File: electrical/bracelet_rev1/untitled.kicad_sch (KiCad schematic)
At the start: 2 parts, among them U9 nRF7002-QFXX

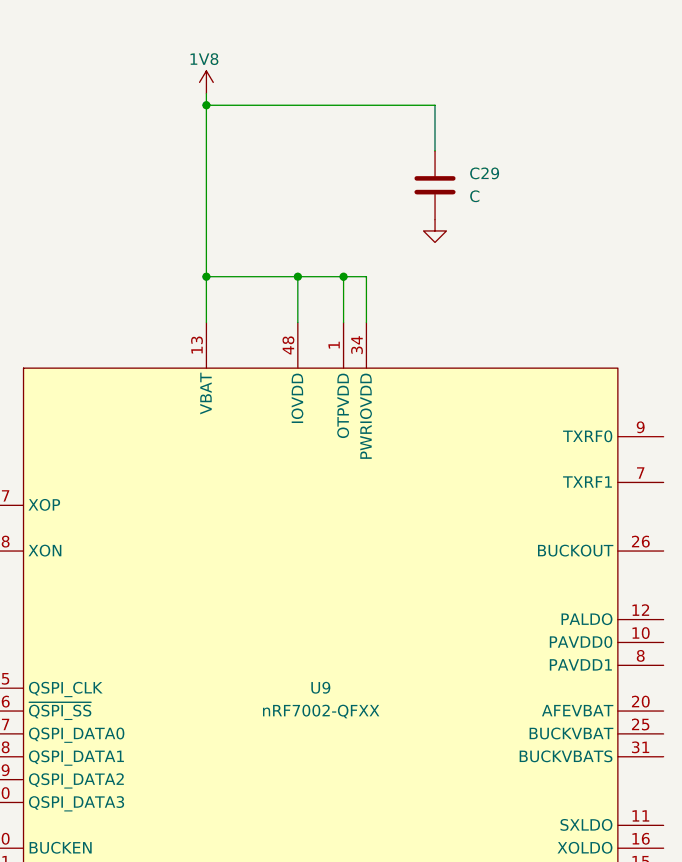
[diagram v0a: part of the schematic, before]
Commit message: Redo component numbers
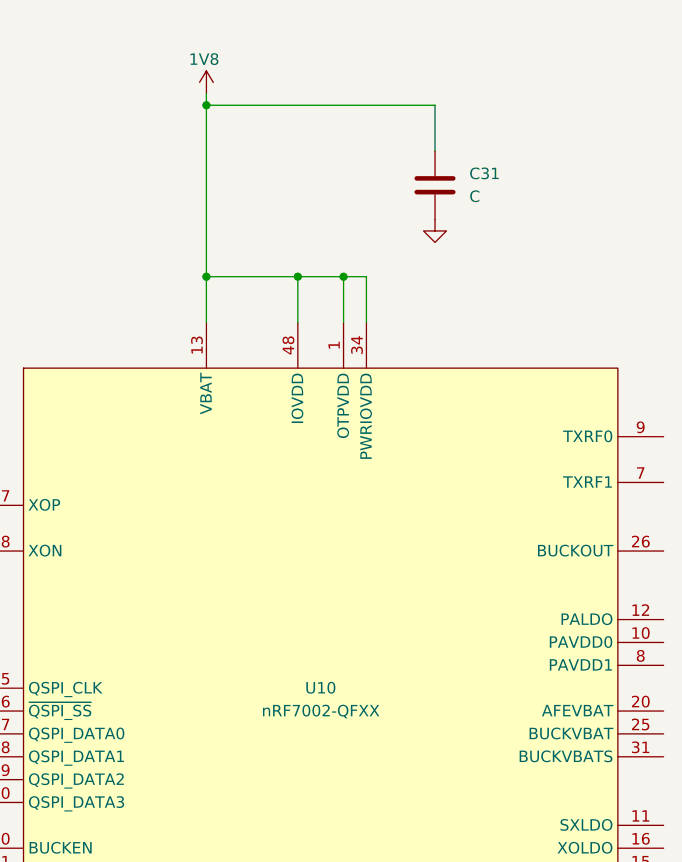
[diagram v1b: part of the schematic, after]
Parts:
- renumbered C29 to C31, U9 to U10
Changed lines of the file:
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@@
 		(dnp no)
 		(fields_autoplaced yes)
-		(property "Reference" "#PWR043"
+		(property "Reference" "#PWR?"
 			(at 152.4 52.07 0)
 			(effects
@@
 			(project "bracelet_rev1"
 				(path "/2a7dd2e8-59c9-4d04-9427-958ca4ea7daa/3d584547-2e56-41a9-bdec-87f8247f577d"
-					(reference "#PWR043")
+					(reference "#PWR?")
 					(unit 1)
 				)
@@
 		(on_board yes)
 		(dnp no)
-		(property "Reference" "#PWR067"
+		(property "Reference" "#PWR?"
 			(at 34.29 26.67 0)
 			(effects
@@
 			(project "bracelet_rev1"
 				(path "/2a7dd2e8-59c9-4d04-9427-958ca4ea7daa/3d584547-2e56-41a9-bdec-87f8247f577d"
-					(reference "#PWR067")
+					(reference "#PWR?")
 					(unit 1)
 				)
@@
 		(dnp no)
 		(fields_autoplaced yes)
-		(property "Reference" "#PWR069"
+		(property "Reference" "#PWR?"
 			(at 139.7 144.78 0)
 			(effects
@@
 			(project "bracelet_rev1"
 				(path "/2a7dd2e8-59c9-4d04-9427-958ca4ea7daa/3d584547-2e56-41a9-bdec-87f8247f577d"
-					(reference "#PWR069")
+					(reference "#PWR?")
 					(unit 1)
 				)
@@
 		(dnp no)
 		(fields_autoplaced yes)
-		(property "Reference" "C29"
+		(property "Reference" "C31"
 			(at 156.21 40.6399 0)
 			(effects
@@
 			(project ""
 				(path "/2a7dd2e8-59c9-4d04-9427-958ca4ea7daa/3d584547-2e56-41a9-bdec-87f8247f577d"
-					(reference "C29")
+					(reference "C31")
 					(unit 1)
 				)
@@
 		(dnp no)
 		(fields_autoplaced yes)
-		(property "Reference" "U9"
+		(property "Reference" "U10"
 			(at 139.7 97.79 0)
 			(do_not_autoplace yes)
@@
 			(project "bracelet_rev1"
 				(path "/2a7dd2e8-59c9-4d04-9427-958ca4ea7daa/3d584547-2e56-41a9-bdec-87f8247f577d"
-					(reference "U9")
+					(reference "U10")
 					(unit 1)
 				)
@@
 		(on_board yes)
 		(dnp no)
-		(property "Reference" "#PWR068"
+		(property "Reference" "#PWR?"
 			(at 127 35.56 0)
 			(effects
@@
 			(project "bracelet_rev1"
 				(path "/2a7dd2e8-59c9-4d04-9427-958ca4ea7daa/3d584547-2e56-41a9-bdec-87f8247f577d"
-					(reference "#PWR068")
-					(unit 1)
-				)
+					(reference "#PWR?")
+					(unit 1)
+				)

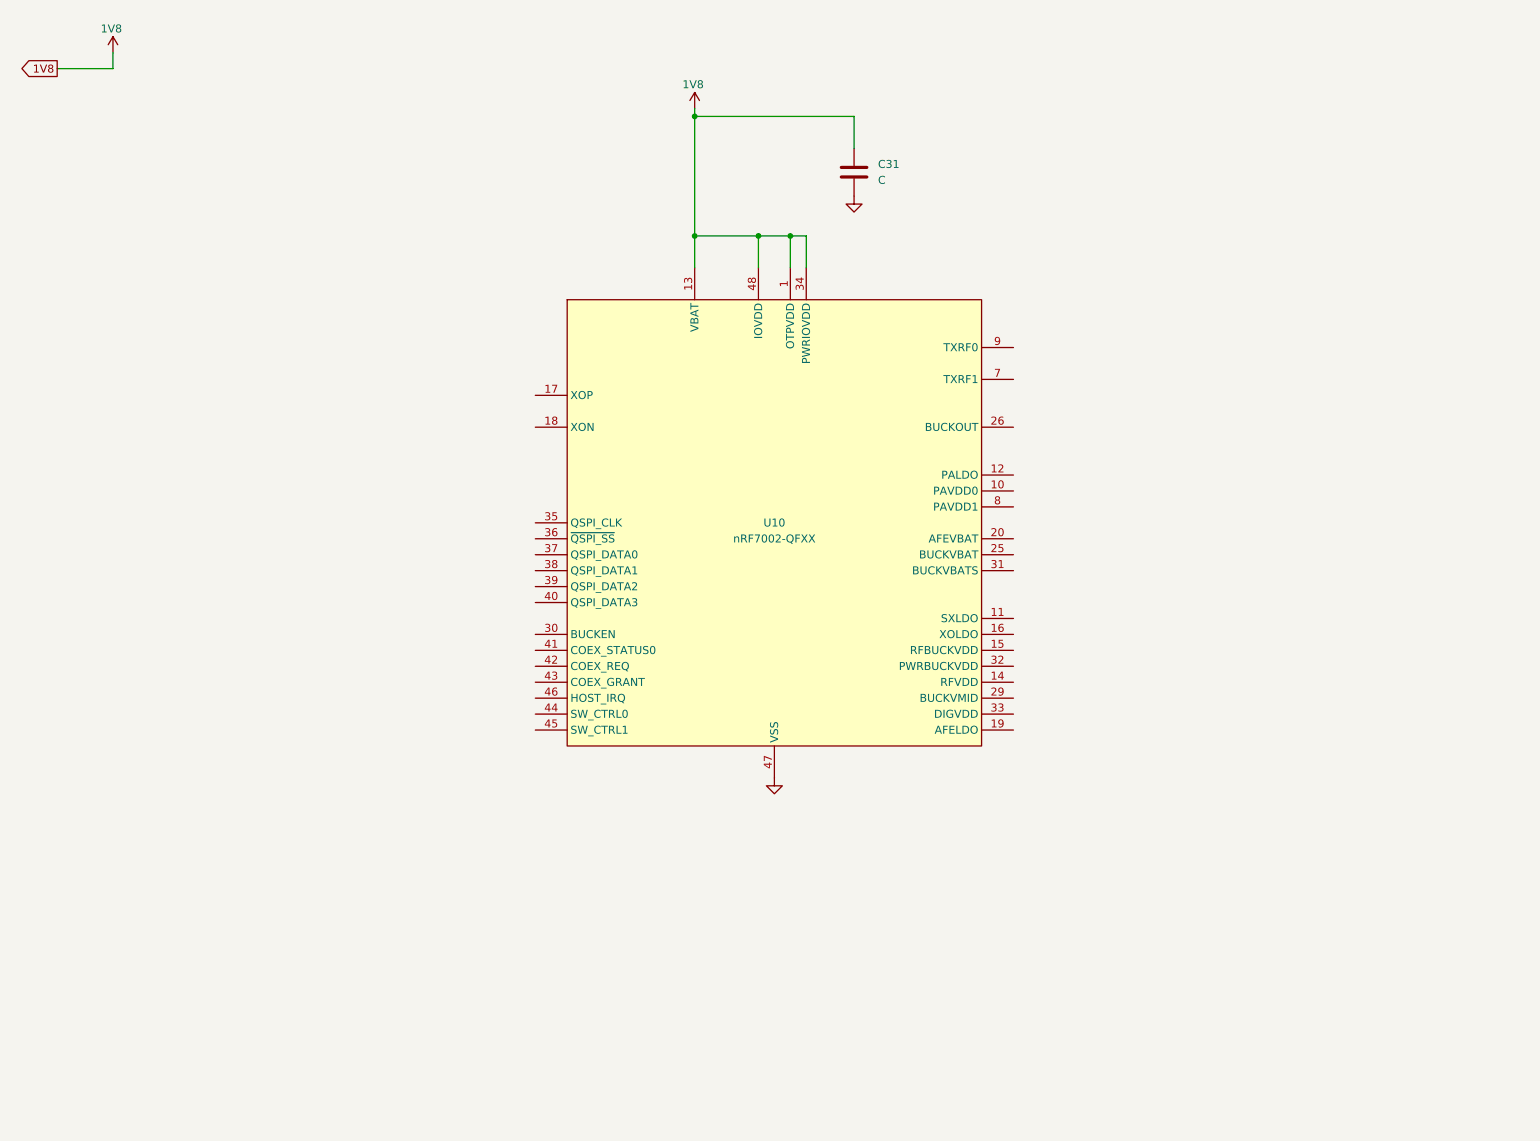
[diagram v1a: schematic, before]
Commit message: Updated Wi-Fi IC
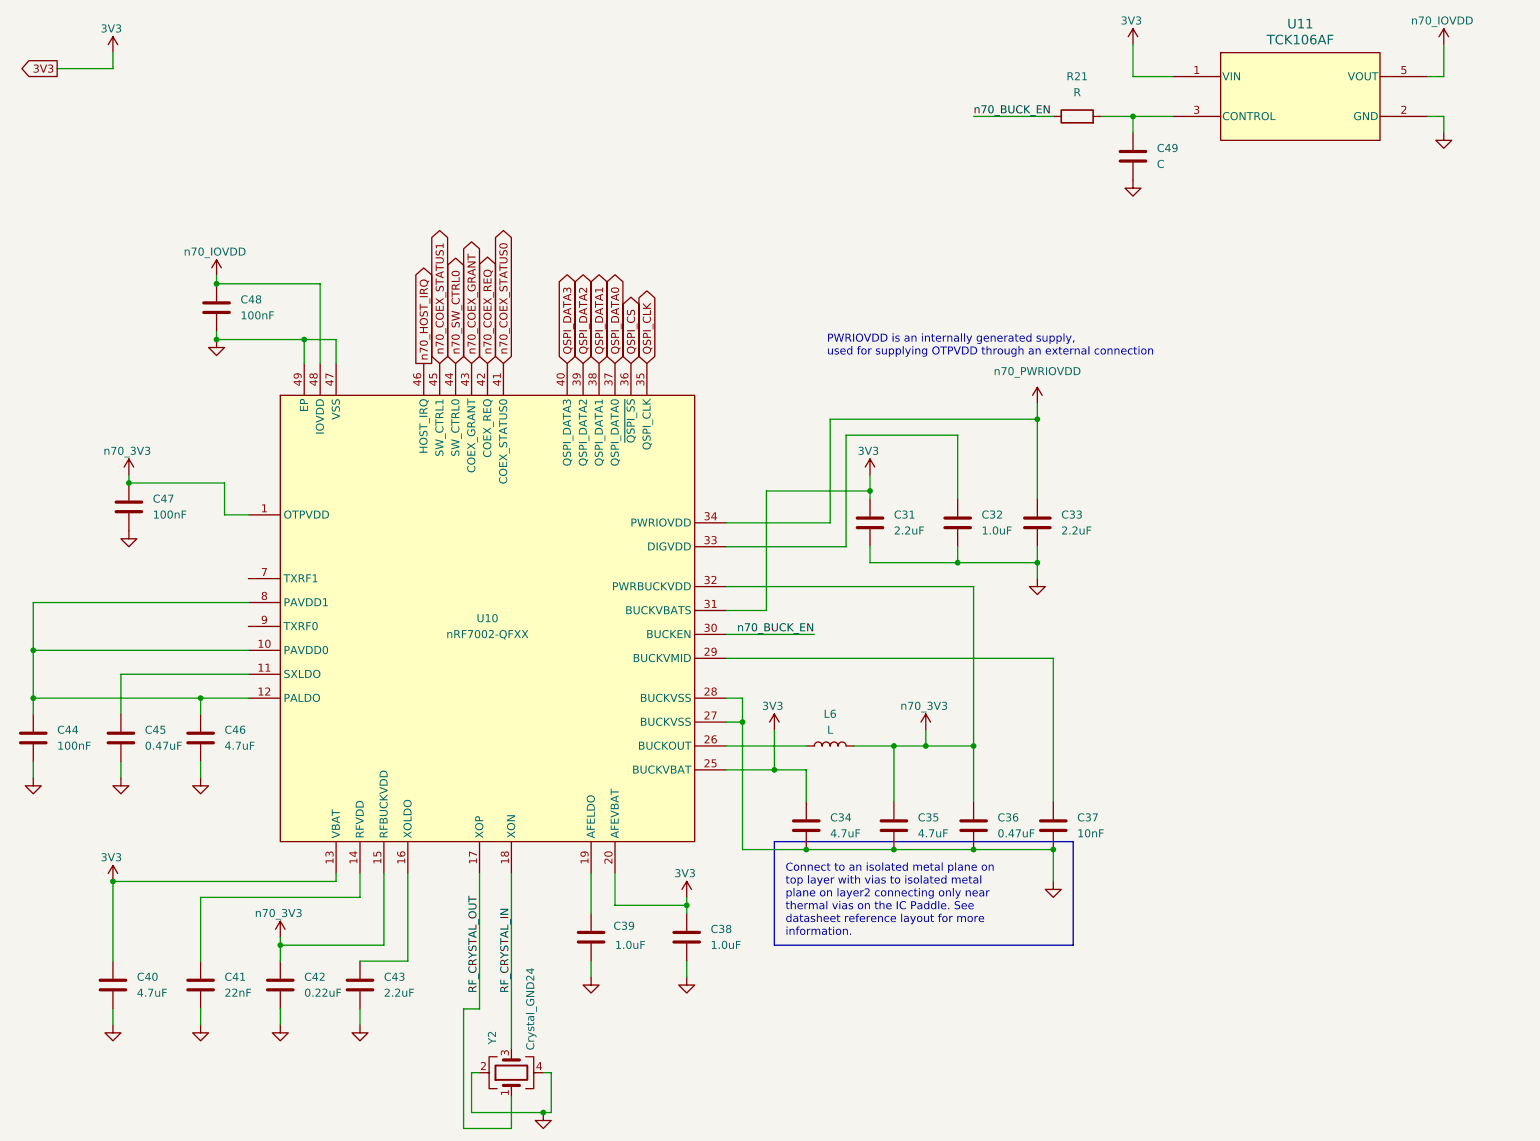
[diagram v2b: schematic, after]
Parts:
- added C32, C38, C39: 1.0uF, symbol Device:C
- added C33, C43: 2.2uF, symbol Device:C
- added C34, C35, C40, C46: 4.7uF, symbol Device:C
- added C36, C45: 0.47uF, symbol Device:C
- added C37: 10nF, symbol Device:C
- added C41: 22nF, symbol Device:C
- added C42: 0.22uF, symbol Device:C
- added C44, C47, C48: 100nF, symbol Device:C
- added C49: C, symbol Device:C
- added L6: L, symbol Device:L
- added R21: R, symbol Device:R
- added U11: TCK106AF, SOT-25_SMV_TOS, symbol TCK106AF:TCK106AF
- added Y2: Crystal_GND24, symbol Device:Crystal_GND24
- C31: value C -> 2.2uF
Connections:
- net GND: now also C32.2, C33.2, C34.2, C35.2, C36.2, C37.2, C38.2, C39.2, C40.2, C41.2, C42.2, C43.2, C44.2, C45.2, C46.2, C47.2, C48.2, C49.2, U11.2 (GND), Y2.2, Y2.4
- net at U10.10 (PAVDD0): now also U10.12 (PALDO), U10.8 (PAVDD1), C44.1, C46.1
- net at U10.11 (SXLDO): now also C45.1
- net at U10.14 (RFVDD): now also C41.1
- net n70_3V3: now reaches U10.15 (RFBUCKVDD)
- net n70_3V3: now also U10.1 (OTPVDD), U10.32 (PWRBUCKVDD), C35.1, C36.1, C42.1, C47.1, L6.2
- net at U10.16 (XOLDO): now also C43.1
- net RF_CRYSTAL_OUT: now reaches U10.17 (XOP)
- net RF_CRYSTAL_OUT: now also Y2.1
- net RF_CRYSTAL_IN: now reaches U10.18 (XON)
- net RF_CRYSTAL_IN: now also Y2.3
- net at U10.19 (AFELDO): now also C39.1
- net 3V3: now reaches U10.20 (AFEVBAT)
- net 3V3: now also C31.1, U10.13 (VBAT), U10.25 (BUCKVBAT), U10.31 (BUCKVBATS), C34.1, C38.1, C40.1, U11.1 (VIN)
- net at U10.26 (BUCKOUT): now also L6.1
- net at U10.29 (BUCKVMID): now also C37.1
- net n70_BUCK_EN: now reaches U10.30 (BUCKEN)
- net n70_BUCK_EN: now also R21.1
- net at U10.33 (DIGVDD): now also C32.1
- net QSPI_CLK: now reaches U10.35 (QSPI_CLK)
- net QSPI_CS: now reaches U10.36 (~{QSPI_SS})
- net QSPI_DATA0: now reaches U10.37 (QSPI_DATA0)
- net QSPI_DATA1: now reaches U10.38 (QSPI_DATA1)
- net QSPI_DATA2: now reaches U10.39 (QSPI_DATA2)
- net QSPI_DATA3: now reaches U10.40 (QSPI_DATA3)
- net n70_COEX_STATUS0: now reaches U10.41 (COEX_STATUS0)
- net n70_COEX_REQ: now reaches U10.42 (COEX_REQ)
- net n70_COEX_GRANT: now reaches U10.43 (COEX_GRANT)
- net n70_SW_CTRL0: now reaches U10.44 (SW_CTRL0)
- net n70_COEX_STATUS1: now reaches U10.45 (SW_CTRL1)
- net n70_HOST_IRQ: now reaches U10.46 (HOST_IRQ)
- removed net 1V8: C31.1, U10.1 (OTPVDD), U10.13 (VBAT), U10.34 (PWRIOVDD), U10.48 (IOVDD)
- new net: C49.1, R21.2, U11.3 (CONTROL)
- new net n70_IOVDD: C48.1, U10.48 (IOVDD), U11.5 (VOUT)
- new net n70_PWRIOVDD: C33.1, U10.34 (PWRIOVDD)
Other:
- note added: "Connect to an isolated metal plane on top layer with vias to isolated metal plane on layer2 connecting only near thermal vias on the IC Paddle. See datasheet reference layout for more information."
- note added: "PWRIOVDD is an internally generated supply, used for supplying OTPVDD through an external connection"

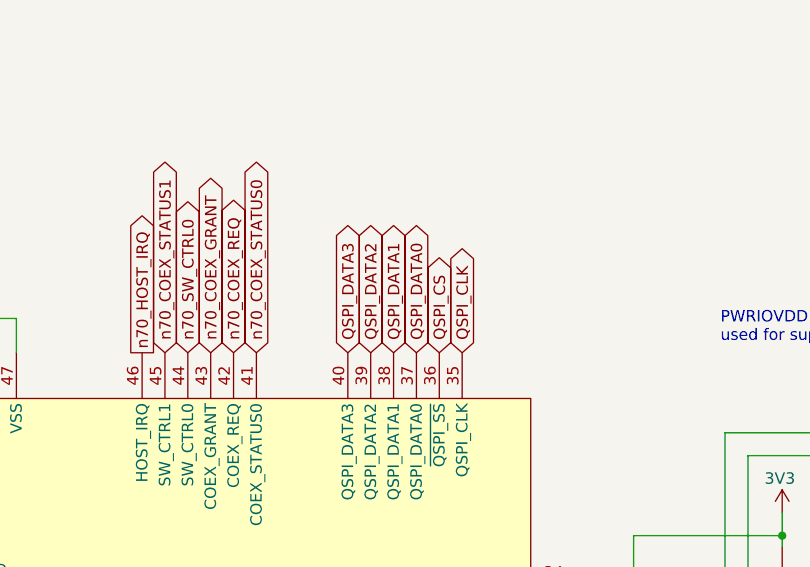
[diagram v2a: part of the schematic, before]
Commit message: Setting up nRF54 pinout
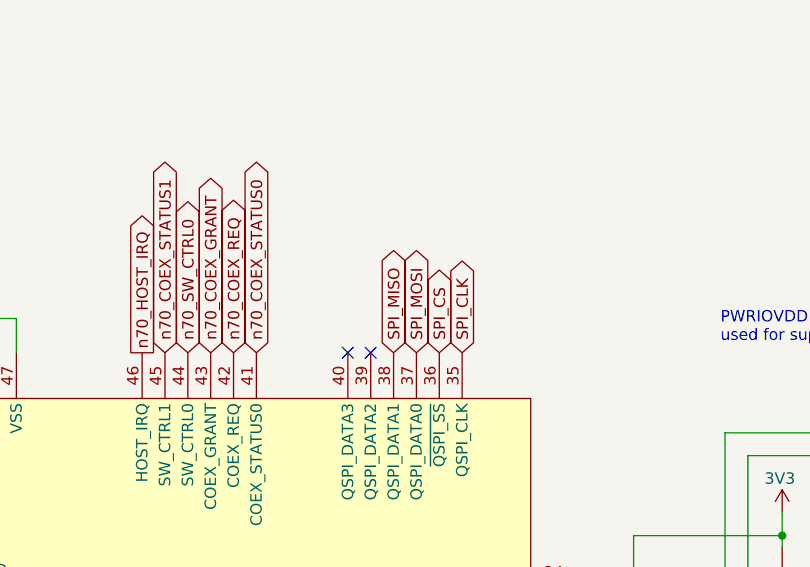
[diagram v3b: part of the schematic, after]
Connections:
- net QSPI_CLK renamed SPI_CLK
- net QSPI_CS renamed SPI_CS
- net QSPI_DATA0 renamed SPI_MOSI
- net QSPI_DATA1 renamed SPI_MISO
- net QSPI_DATA2: no longer names the net of U10.39 (QSPI_DATA2)
- net QSPI_DATA3: no longer names the net of U10.40 (QSPI_DATA3)
- no-connect marks 0 -> 2
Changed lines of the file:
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@@
 		(color 0 0 0 0)
+	)
+	(no_connect
+		(at 106.68 72.39)
+	)
+	(no_connect
+		(at 109.22 72.39)
 	)
 	(wire
@@
 		)
 	)
-	(global_label "QSPI_DATA0"
+	(global_label "SPI_MOSI"
 		(shape bidirectional)
 		(at 114.3 72.39 90)
@@
 		)
 		(property "Intersheetrefs" "${INTERSHEET_REFS}"
-			(at 114.3 57.2868 90)
-			(effects
-				(font
-					(size 1.27 1.27)
-				)
-				(justify left)
-				(hide yes)
-			)
-		)
-	)
-	(global_label "QSPI_DATA3"
-		(shape bidirectional)
-		(at 106.68 72.39 90)
-		(fields_autoplaced yes)
-		(effects
-			(font
-				(size 1.27 1.27)
-			)
-			(justify left)
-		)
-		(property "Intersheetrefs" "${INTERSHEET_REFS}"
-			(at 106.68 57.2868 90)
+			(at 114.3 59.6454 90)
 			(effects
 				(font
@@
 		)
 	)
-	(global_label "QSPI_DATA2"
-		(shape bidirectional)
-		(at 109.22 72.39 90)
-		(fields_autoplaced yes)
-		(effects
-			(font
-				(size 1.27 1.27)
-			)
-			(justify left)
-		)
-		(property "Intersheetrefs" "${INTERSHEET_REFS}"
-			(at 109.22 57.2868 90)
-			(effects
-				(font
-					(size 1.27 1.27)
-				)
-				(justify left)
-				(hide yes)
-			)
-		)
-	)
-	(global_label "QSPI_CLK"
+	(global_label "SPI_CLK"
 		(shape bidirectional)
 		(at 119.38 72.39 90)
@@
 		)
 		(property "Intersheetrefs" "${INTERSHEET_REFS}"
-			(at 119.38 59.343 90)
+			(at 119.38 60.6735 90)
 			(effects
 				(font
@@
 		)
 	)
-	(global_label "QSPI_CS"
+	(global_label "SPI_CS"
 		(shape bidirectional)
 		(at 116.84 72.39 90)
@@
 		)
 		(property "Intersheetrefs" "${INTERSHEET_REFS}"
-			(at 116.84 60.4316 90)
+			(at 116.84 61.7621 90)
 			(effects
 				(font
@@
 		)
 	)
-	(global_label "QSPI_DATA1"
+	(global_label "SPI_MISO"
 		(shape bidirectional)
 		(at 111.76 72.39 90)
@@
 		)
 		(property "Intersheetrefs" "${INTERSHEET_REFS}"
-			(at 111.76 57.2868 90)
+			(at 111.76 59.6454 90)
 			(effects
 				(font

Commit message: More schematic stuff
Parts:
- added AE2: 206514-0001, symbol Device:Antenna_Chip
- added U12: ~, symbol LFD182G45DCHD277:LFD182G45DCHD277
- C31, C32, C33, C34, C35, C36, C37, C38, C39, C40, C41, C42, C43, C44, C45, C46, C47, C48: footprint (none) -> Capacitor_SMD:C_0603_1608Metric_Pad1.08x0.95mm_HandSolder
- C49: value C -> 1.0uF; footprint (none) -> Capacitor_SMD:C_0603_1608Metric_Pad1.08x0.95mm_HandSolder
- L6: value L -> 3.3uH; footprint (none) -> Inductor_SMD:L_0603_1608Metric_Pad1.05x0.95mm_HandSolder
- R21: footprint (none) -> Resistor_SMD:R_0201_0603Metric_Pad0.64x0.40mm_HandSolder
- U11: footprint SOT-25_SMV_TOS -> (none)
- Y2: footprint (none) -> Crystal:Crystal_SMD_3225-4Pin_3.2x2.5mm_HandSoldering
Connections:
- net GND: now also AE2.2 (PCB_Trace), U12.2 (GND), U12.5 (GND), U12.7 (GND)
- net at U10.7 (TXRF1): now also U12.3 (P2_HF)
- net at U10.9 (TXRF0): now also U12.1 (P1_LF)
- new net: AE2.1 (FEED), U12.6 (P3_RFC)
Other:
- moved on the sheet: C31, C32, C33, C34, C35, C36, C37, C38, C39, C40, C41, C42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
